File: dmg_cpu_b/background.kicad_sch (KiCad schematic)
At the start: 76 parts

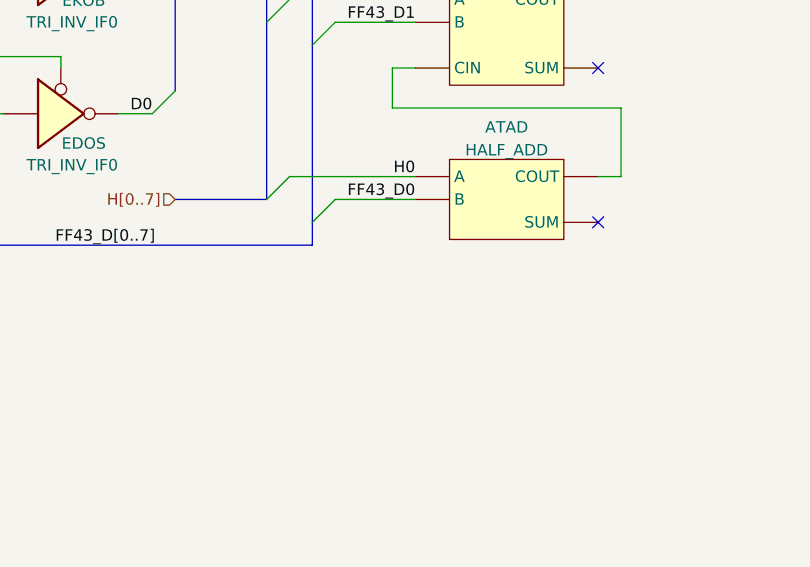
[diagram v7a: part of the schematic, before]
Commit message: Elements from sptite control sheet moved to lcd sheet.
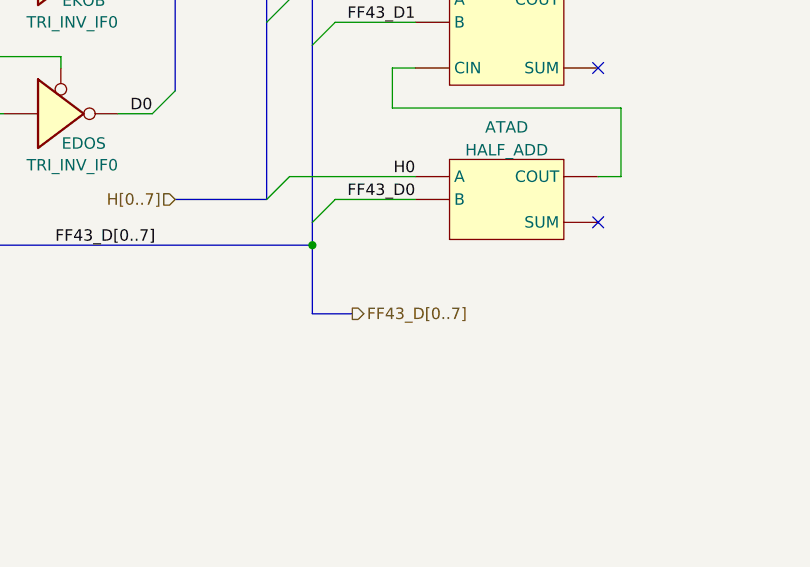
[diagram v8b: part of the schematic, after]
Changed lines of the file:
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@@
   (junction (at 256.54 111.76) (diameter 0) (color 0 0 0 0)
+  )
+  (junction (at 330.835 176.53) (diameter 0) (color 0 0 0 0)
   )
   (junction (at 391.16 15.875) (diameter 0) (color 0 0 0 0)
@@
     (stroke (width 0) (type default) (color 0 0 0 0))
   )
+  (bus (pts (xy 330.835 176.53) (xy 330.835 184.15))
+    (stroke (width 0) (type default) (color 0 0 0 0))
+  )
   (bus (pts (xy 291.465 48.26) (xy 291.465 64.135))
     (stroke (width 0) (type default) (color 0 0 0 0))
@@
   )
   (wire (pts (xy 75.565 41.275) (xy 78.105 41.275))
+    (stroke (width 0) (type default) (color 0 0 0 0))
+  )
+  (bus (pts (xy 330.835 184.15) (xy 335.28 184.15))
     (stroke (width 0) (type default) (color 0 0 0 0))
   )
@@
     (effects (font (size 1.27 1.27)) (justify right))
   )
+  (hierarchical_label "FF43_D[0..7]" (shape output) (at 335.28 184.15 0)
+    (effects (font (size 1.27 1.27)) (justify left))
+  )
   (hierarchical_label "BP_SEL" (shape input) (at 156.21 238.76 180)
